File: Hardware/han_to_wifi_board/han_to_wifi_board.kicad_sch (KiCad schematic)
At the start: 38 parts, among them IC1 MIC2779L-2YM5_TR, J1 RJLSE4118101, J2 Conn_01x04_Male, SW1 RESET, U1 ESP-12F, U2 LT8619, U3 NCN5150

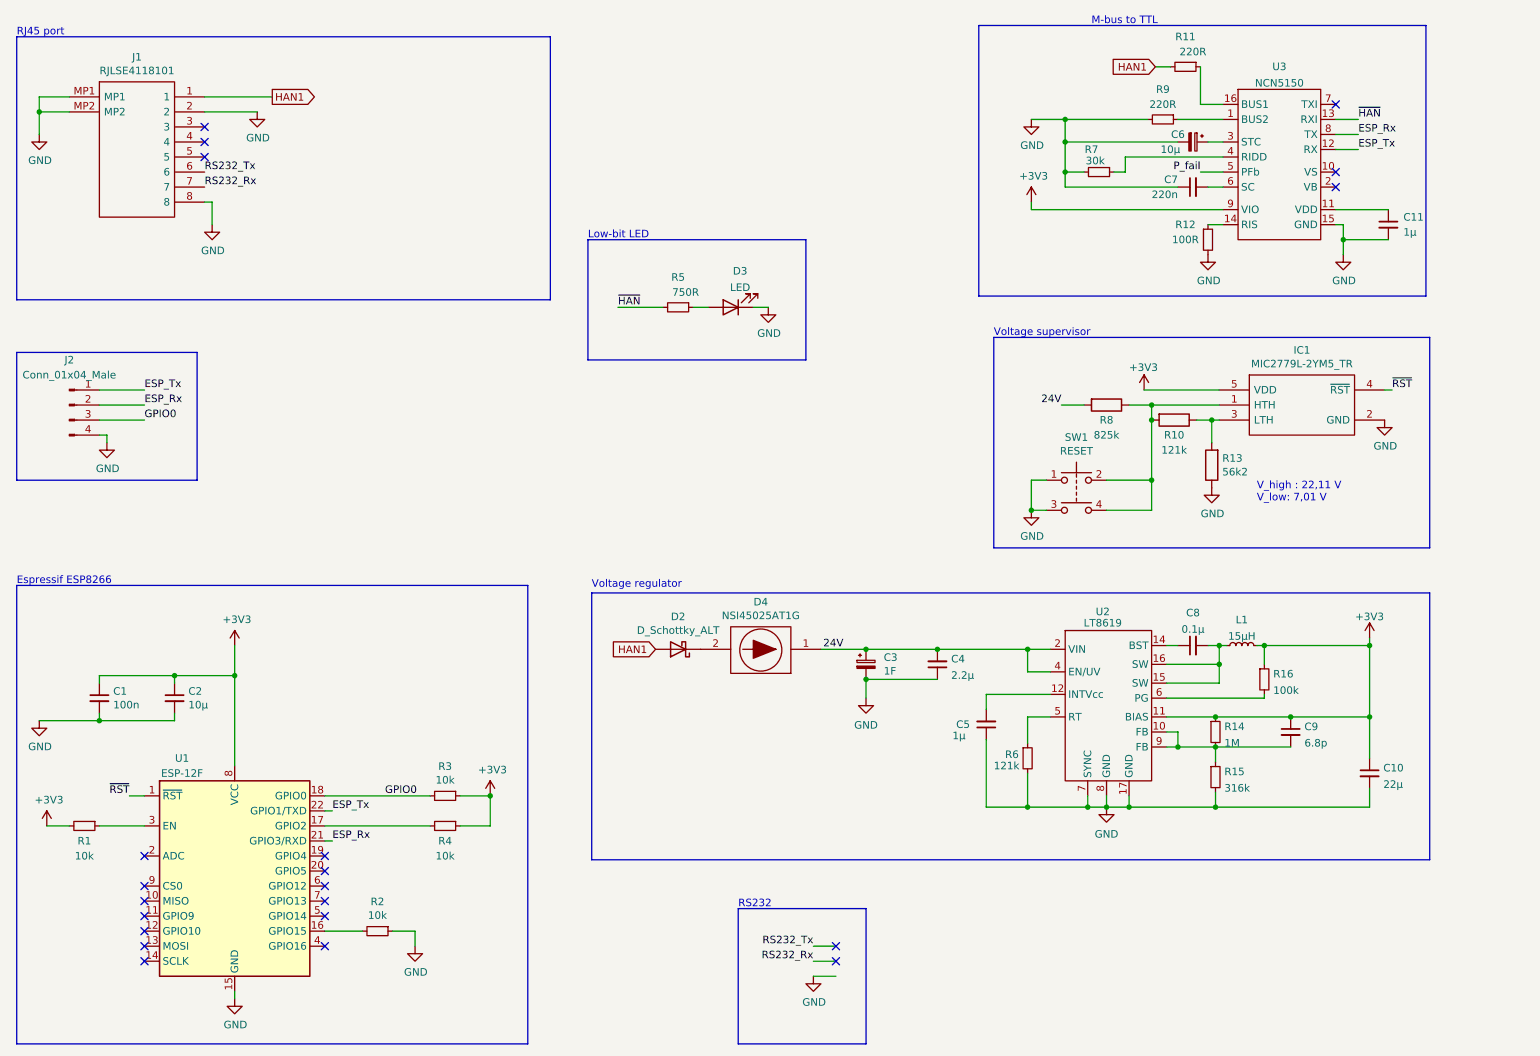
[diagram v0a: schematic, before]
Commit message: New buck converter
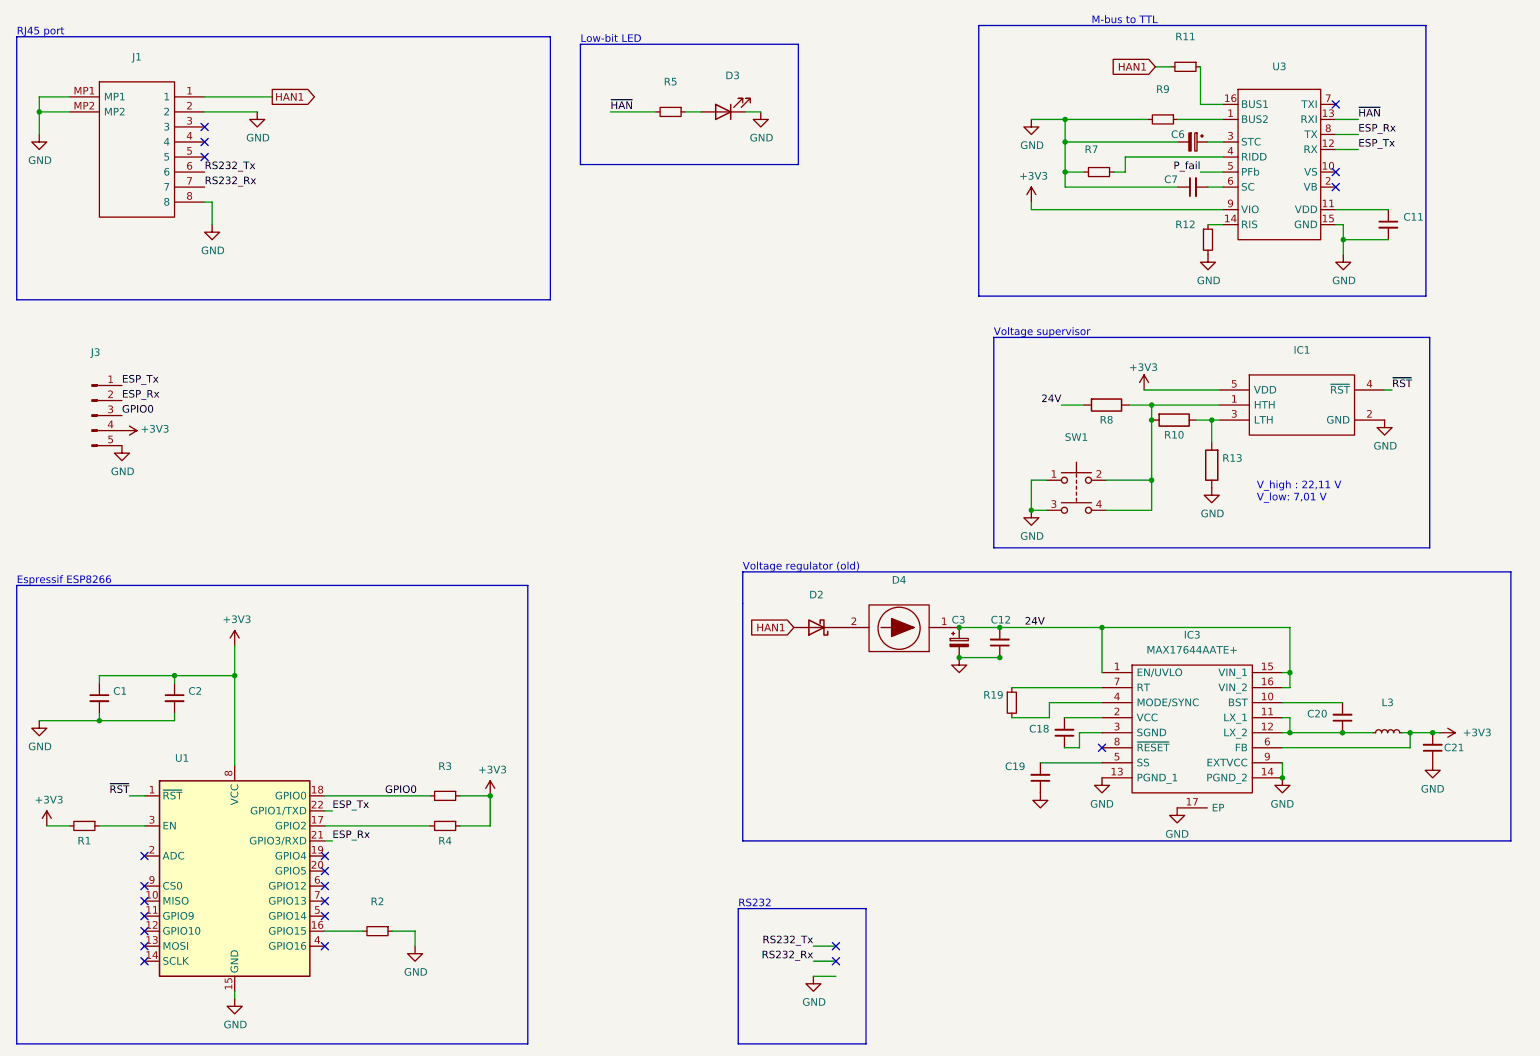
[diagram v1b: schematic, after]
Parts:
- removed C10: 22µ, Capacitor_SMD:C_0603_1608Metric, symbol Device:C_Small
- removed C4: 2.2µ, Capacitor_SMD:C_0805_2012Metric, symbol Device:C_Small
- removed C5: 1µ, Capacitor_SMD:C_0805_2012Metric, symbol Device:C_Small
- removed C8: 0.1µ, Capacitor_SMD:C_0603_1608Metric, symbol Device:C_Small
- removed C9: 6.8p, Capacitor_SMD:C_0402_1005Metric, symbol Device:C_Small
- removed J2: Conn_01x04_Male, TSM-104-02-S-SH-001:TSM10402SSH001, symbol Connector:Conn_01x04_Male
- removed L1: 15µH, Inductor_SMD:L_0603_1608Metric, symbol Device:L_Small
- removed R14: 1M, Resistor_SMD:R_0402_1005Metric, symbol Device:R_Small
- removed R15: 316k, Resistor_SMD:R_0603_1608Metric, symbol Device:R_Small
- removed R16: 100k, Resistor_SMD:R_0402_1005Metric, symbol Device:R_Small
- removed R6: 121k, Resistor_SMD:R_0402_1005Metric, symbol Device:R_Small
- removed U2: LT8619, LIB_LT8619EMSE-5#PBF:SOP50P490X110-17N, symbol LT8619:LT8619
- added C12, C18, C19, C20, C21: (no value), symbol Device:C_Small
- added IC3: MAX17644AATE+, QFN50P300X300X80-17N, symbol MAX17644AATE+:MAX17644AATE+
- added J3: (no value), symbol Connector:Conn_01x05_Male
- added L3: (no value), symbol Device:L_Small
- added R19: (no value), symbol Device:R_Small
- C1: value 100n -> (none); footprint Capacitor_SMD:C_0603_1608Metric -> (none)
- C11: value 1µ -> (none); footprint Capacitor_SMD:C_0805_2012Metric -> (none)
- C2, C6: value 10µ -> (none); footprint Capacitor_SMD:C_0603_1608Metric -> (none)
- C3: value 1F -> (none); footprint MAL202117102E3:MAL202117102E3 -> (none)
- C7: value 220n -> (none); footprint Capacitor_SMD:C_0603_1608Metric -> (none)
- D2: value D_Schottky_ALT -> (none); footprint Diode_SMD:D_0402_1005Metric -> (none)
- D3: value LED -> (none); footprint LED_SMD:LED_0603_1608Metric -> (none)
- D4: value NSI45025AT1G -> (none); footprint NSI45025AT1G:NSI45025AT1G -> (none)
- IC1: value MIC2779L-2YM5_TR -> (none); footprint MIC2779L:SOT95P280X145-5N -> (none)
- J1: value RJLSE4118101 -> (none); footprint RJLSE4118101:RJLSE4118101 -> (none)
- R1, R2, R3, R4: value 10k -> (none); footprint Resistor_SMD:R_0402_1005Metric -> (none)
- R10: value 121k -> (none); footprint Resistor_SMD:R_0402_1005Metric -> (none)
- R11, R9: value 220R -> (none); footprint Resistor_SMD:R_0603_1608Metric -> (none)
- R12: value 100R -> (none); footprint Resistor_SMD:R_0603_1608Metric -> (none)
- R13: value 56k2 -> (none); footprint Resistor_SMD:R_0402_1005Metric -> (none)
- R5: value 750R -> (none); footprint Resistor_SMD:R_0603_1608Metric -> (none)
- R7: value 30k -> (none); footprint Resistor_SMD:R_0402_1005Metric -> (none)
- R8: value 825k -> (none); footprint Resistor_SMD:R_0402_1005Metric -> (none)
- SW1: value RESET -> (none); footprint Button_Switch_SMD:SW_SPST_EVQP2 -> (none)
- U1: value ESP-12F -> (none); footprint RF_Module:ESP-12E -> (none)
- U3: value NCN5150 -> (none); footprint NCN5150DR2G:SOIC127P600X175-16N -> (none)
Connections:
- net +3V3: now also C21.2, IC3.6 (FB), J3.4 (Pin_4), L3.2
- net 24V: now also C12.2, IC3.1 (EN/UVLO), IC3.15 (VIN_1), IC3.16 (VIN_2)
- net ESP_Rx: now also J3.2 (Pin_2)
- net ESP_Tx: now also J3.1 (Pin_1)
- net GND: now also C12.1, C19.1, C21.1, IC3.13 (PGND_1), IC3.14 (PGND_2), IC3.17 (EP), IC3.9 (EXTVCC), J3.5 (Pin_5)
- net GPIO0: now also J3.3 (Pin_3)
- new net: C18.1, IC3.3 (SGND)
- new net: C18.2, IC3.2 (VCC)
- new net: C20.2, IC3.10 (BST)
- new net: C20.1, IC3.11 (LX_1), IC3.12 (LX_2), L3.1
- new net: IC3.4 (MODE/SYNC), R19.2
- new net: C19.2, IC3.5 (SS)
- new net: IC3.7 (RT), R19.1
- no-connect marks 21 -> 22
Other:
- note added: "Voltage regulator (old)"
- note removed: "Voltage regulator"
- moved on the sheet: C3, D2, D3, D4, R5

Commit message: Connected SGND on buck to GND
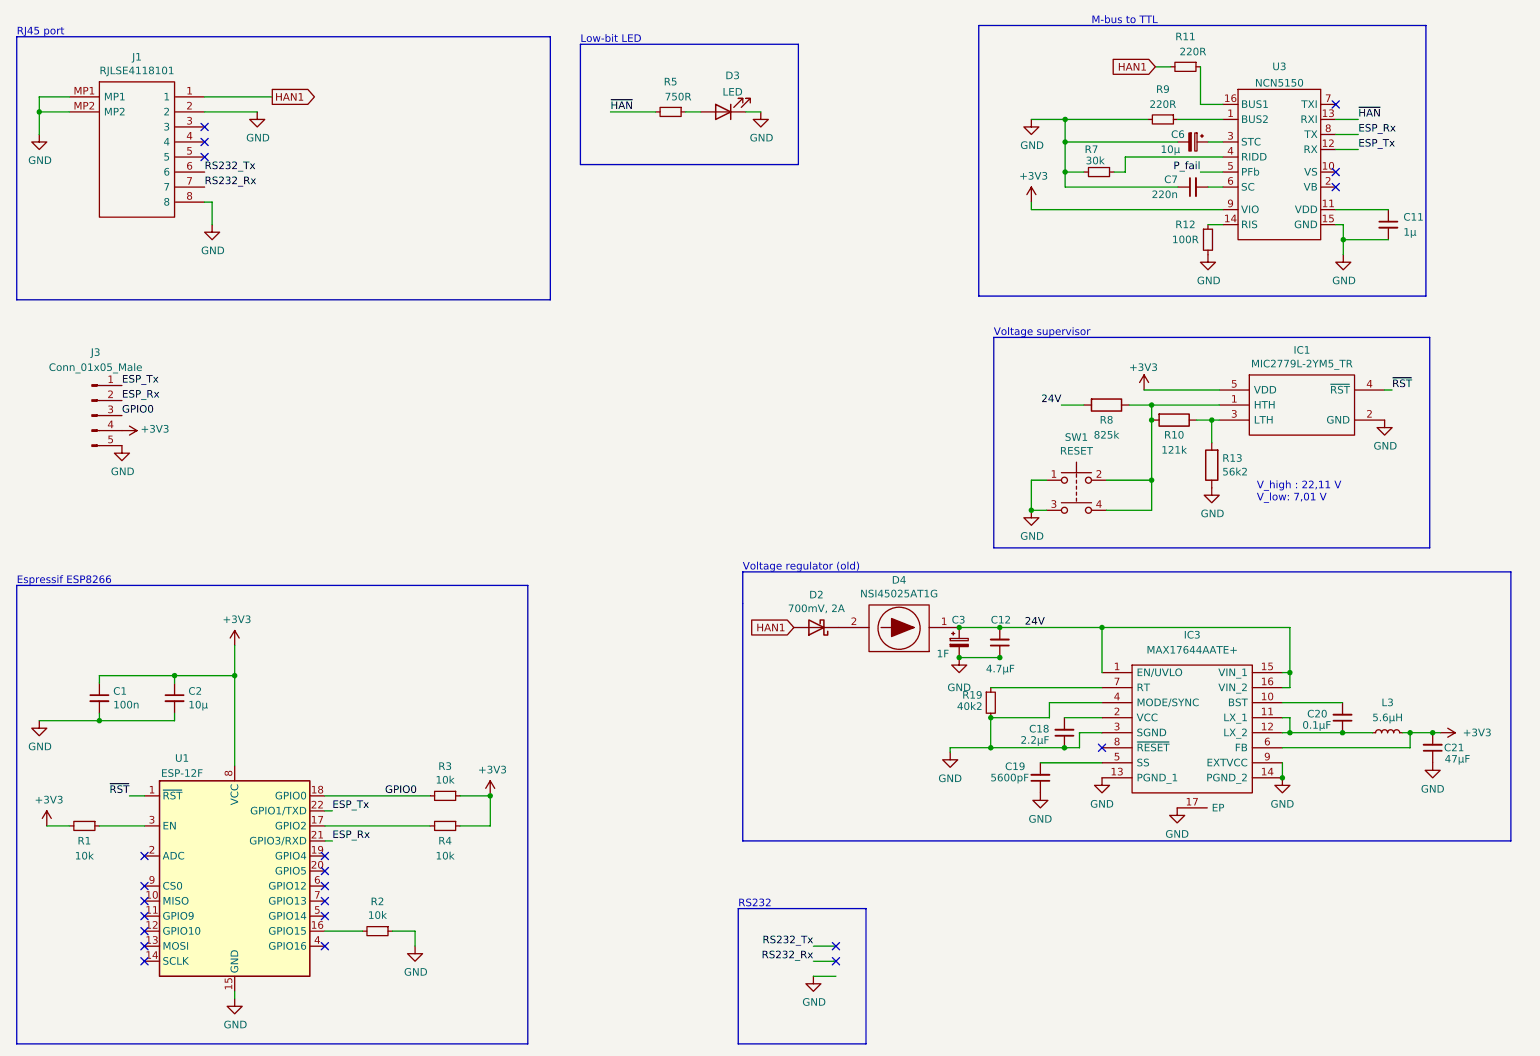
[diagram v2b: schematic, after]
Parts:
- C1: value (none) -> 100n; footprint (none) -> Capacitor_SMD:C_0603_1608Metric
- C11: value (none) -> 1µ; footprint (none) -> Capacitor_SMD:C_0805_2012Metric
- C12: value (none) -> 4.7µF; footprint (none) -> Capacitor_SMD:C_0805_2012Metric
- C18: value (none) -> 2.2µF; footprint (none) -> Capacitor_SMD:C_0603_1608Metric
- C19: value (none) -> 5600pF; footprint (none) -> Capacitor_SMD:C_0603_1608Metric
- C2, C6: value (none) -> 10µ; footprint (none) -> Capacitor_SMD:C_0603_1608Metric
- C20: value (none) -> 0.1µF; footprint (none) -> Capacitor_SMD:C_0603_1608Metric
- C21: value (none) -> 47µF; footprint (none) -> Capacitor_SMD:C_0805_2012Metric
- C3: value (none) -> 1F; footprint (none) -> MAL202117102E3:MAL202117102E3
- C7: value (none) -> 220n; footprint (none) -> Capacitor_SMD:C_0603_1608Metric
- D2: value (none) -> 700mV, 2A; footprint (none) -> Diode_SMD:D_SMA
- D3: value (none) -> LED; footprint (none) -> LED_SMD:LED_0603_1608Metric
- D4: value (none) -> NSI45025AT1G; footprint (none) -> NSI45025AT1G:NSI45025AT1G
- IC1: value (none) -> MIC2779L-2YM5_TR; footprint (none) -> MIC2779L:SOT95P280X145-5N
- J1: value (none) -> RJLSE4118101; footprint (none) -> RJLSE4118101:RJLSE4118101
- J3: value (none) -> Conn_01x05_Male; footprint (none) -> Connector_Molex:Molex_PicoBlade_53261-0571_1x05-1MP_P1.25mm_Horizontal
- L3: value (none) -> 5.6µH; footprint (none) -> Inductor_SMD:L_Vishay_IHLP-2020
- R1, R2, R3, R4: value (none) -> 10k; footprint (none) -> Resistor_SMD:R_0402_1005Metric
- R10: value (none) -> 121k; footprint (none) -> Resistor_SMD:R_0402_1005Metric
- R11, R9: value (none) -> 220R; footprint (none) -> Resistor_SMD:R_0603_1608Metric
- R12: value (none) -> 100R; footprint (none) -> Resistor_SMD:R_0603_1608Metric
- R13: value (none) -> 56k2; footprint (none) -> Resistor_SMD:R_0402_1005Metric
- R19: value (none) -> 40k2; footprint (none) -> Resistor_SMD:R_0603_1608Metric
- R5: value (none) -> 750R; footprint (none) -> Resistor_SMD:R_0603_1608Metric
- R7: value (none) -> 30k; footprint (none) -> Resistor_SMD:R_0402_1005Metric
- R8: value (none) -> 825k; footprint (none) -> Resistor_SMD:R_0402_1005Metric
- SW1: value (none) -> RESET; footprint (none) -> Button_Switch_SMD:SW_SPST_EVQP2
- U1: value (none) -> ESP-12F; footprint (none) -> RF_Module:ESP-12E
- U3: value (none) -> NCN5150; footprint (none) -> NCN5150DR2G:SOIC127P600X175-16N
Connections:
- net GND: now also C18.1, IC3.3 (SGND), IC3.4 (MODE/SYNC), R19.2
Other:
- moved on the sheet: R19

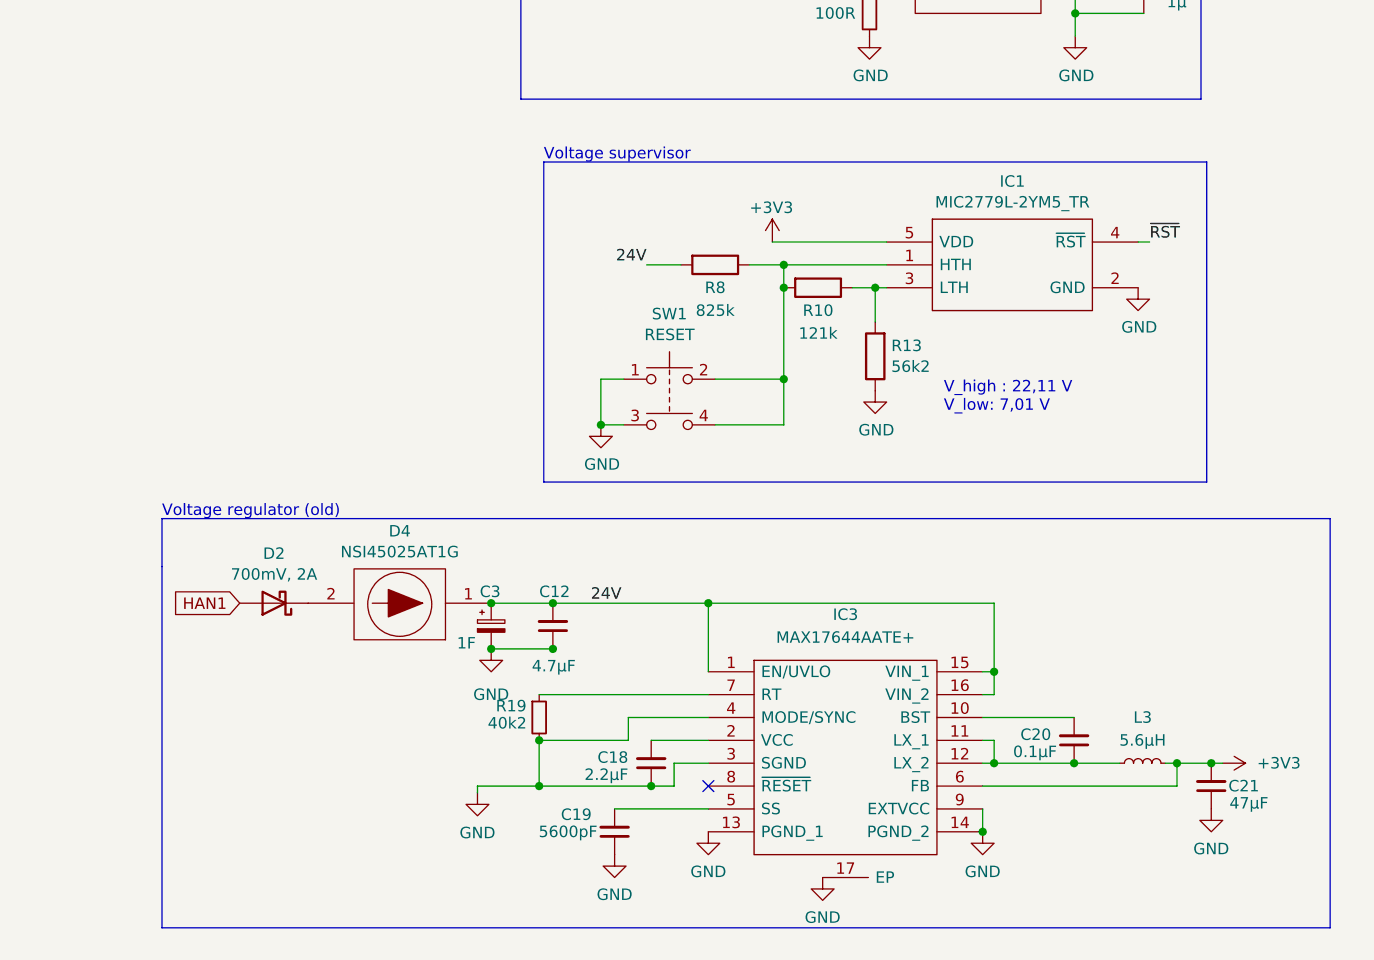
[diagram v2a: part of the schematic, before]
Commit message: Reset pin on buck
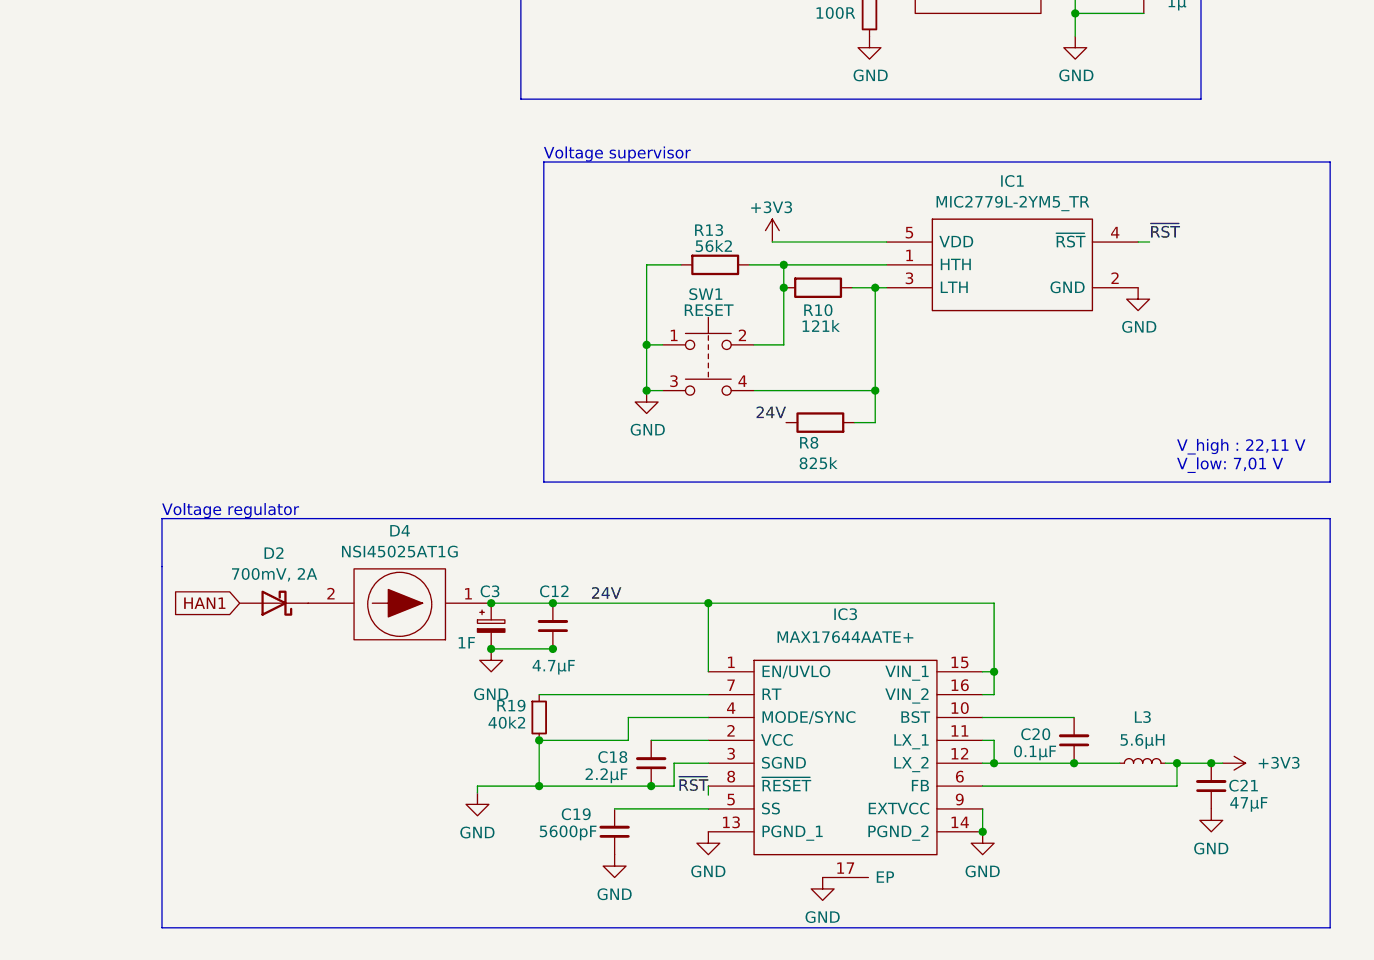
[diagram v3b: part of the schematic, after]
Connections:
- net 24V: now also R8.1; no longer R8.2
- net GND: now also R13.2; no longer R13.1
- net ~{RST}: now also IC3.8 (~{RESET})
- net at IC1.1 (HTH), R10.2, SW1.2: now also R13.1; no longer R8.1, SW1.4
- net at IC1.3 (LTH), R10.1: now also R8.2, SW1.4; no longer R13.2
- no-connect marks 22 -> 21
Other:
- note added: "Voltage regulator"
- note removed: "Voltage regulator (old)"
- moved on the sheet: R13, R8, SW1

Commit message: September hw changes
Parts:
- added SW2: PRGRM, Button_Switch_SMD:SW_SPST_EVQP2, symbol Switch:SW_Push_Dual
- R1, R10, R13, R2, R3, R4, R7, R8: footprint Resistor_SMD:R_0402_1005Metric -> Resistor_SMD:R_0603_1608Metric
- R12: now left out of the parts list
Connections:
- net GND: now also SW2.2; no longer SW1.3
- net GPIO0: now also SW2.1
- net ~{RST}: now also SW1.2; no longer U1.1 (~{RST})
- net at IC1.1 (HTH), R10.2, R13.1: no longer SW1.2
- net at IC1.3 (LTH), R10.1, R8.2: no longer SW1.4
- no-connect marks 21 -> 24
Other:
- note added: "Do not place"
- moved on the sheet: IC1, R10, R13, R8, SW1
